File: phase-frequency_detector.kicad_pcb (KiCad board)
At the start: 2 copper layers, 160 x 100 mm, 89 parts, among them J1 REF, J2 IN, J3 Error_Out, J4 C64AC, J5 Switch, J6 Fast_Out, U1 HMC439QS16G, U2 LT3045EMSE, U3 LT3094EMSE, U4 ADA4896-2ARMZ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

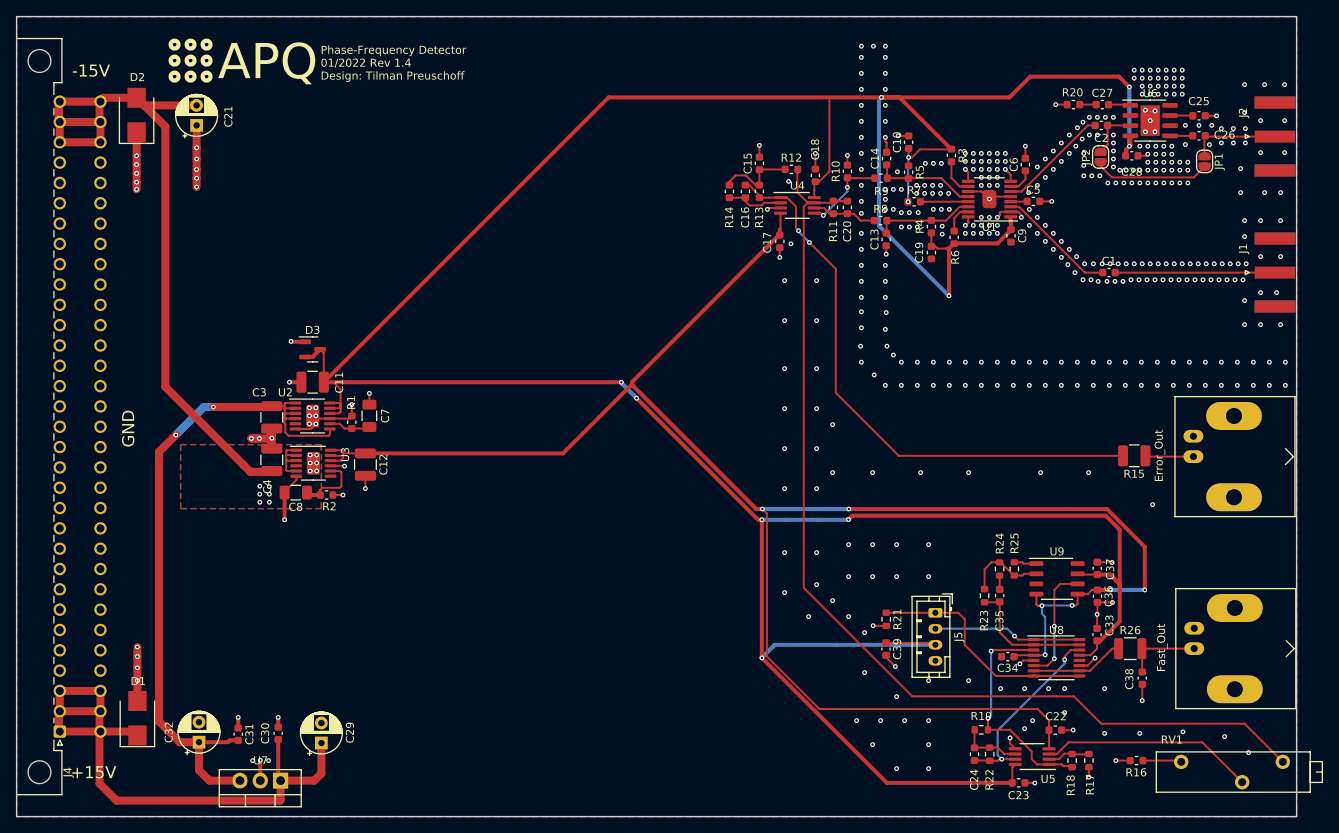
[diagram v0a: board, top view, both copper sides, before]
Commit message: Remove solder paste from DNF footprints.
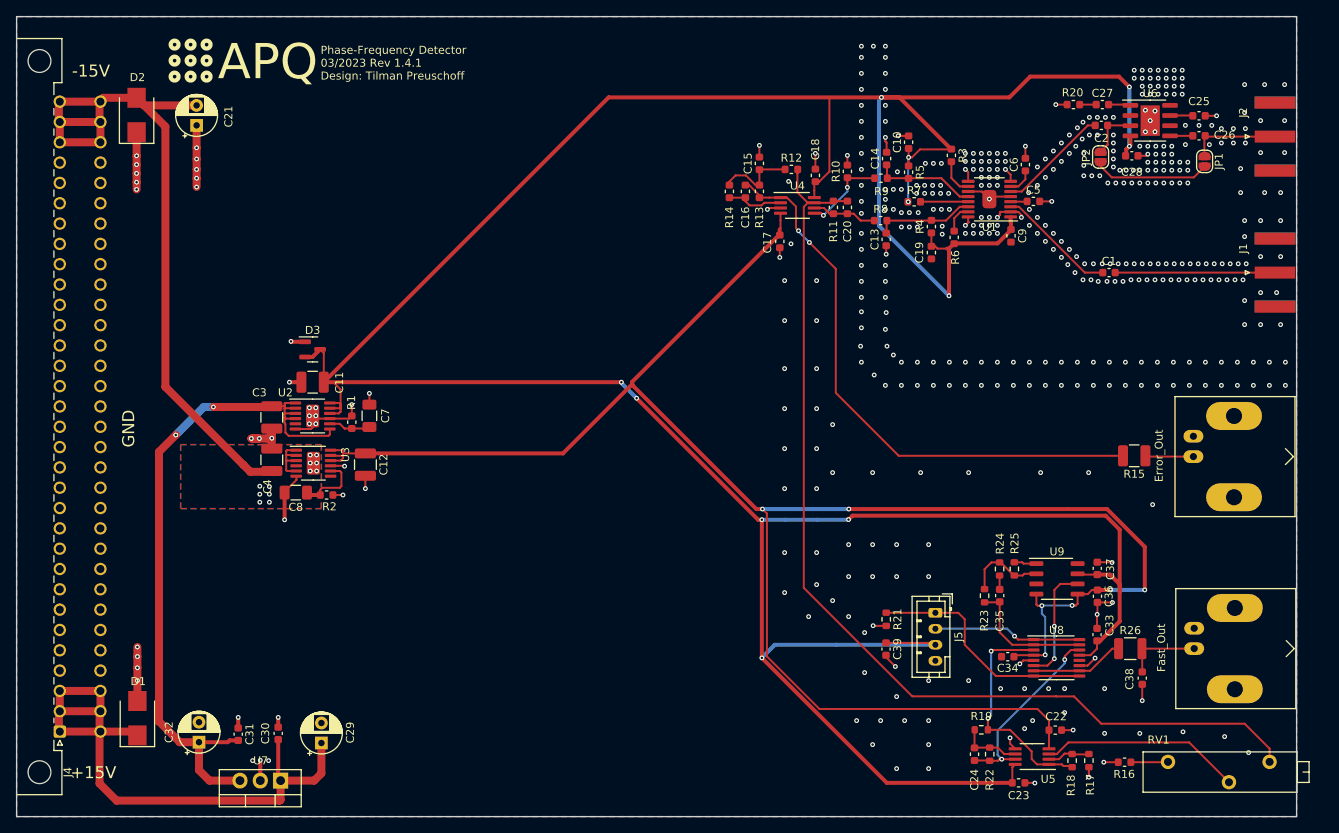
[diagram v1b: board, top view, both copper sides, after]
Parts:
- U1: footprint footprints:QSOP-16_3.9x4.9mm_P0.635mm_EP_2.3mmx1.75mm -> footprints:QSOP-16_3.9x4.9mm_P0.635mm_EP_2.3mmx1.75mm_DNF
- U6: footprint Package_SO:SOIC-8-1EP_3.9x4.9mm_P1.27mm_EP2.41x3.81mm -> footprints:SOIC-8-1EP_3.9x4.9mm_P1.27mm_EP2.41x3.81mm_DNF
- moved RV1 1.66 mm to (213.9, 143.2)
- moved R16 1.52 mm to (208.5, 143.2)
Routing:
- net Net-(RV1-Pad2): track 26.8 -> 25.2 mm
- net /Fast PD regulator/error_sig: track 127.0 -> 126.3 mm
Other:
- board text added: "Phase-Frequency Detector 03/2023 Rev 1.4.1 Design: Tilman Preuschoff"
- board text removed: "Phase-Frequency Detector 01/2022 Rev 1.4 Design: Tilman Preuschoff"

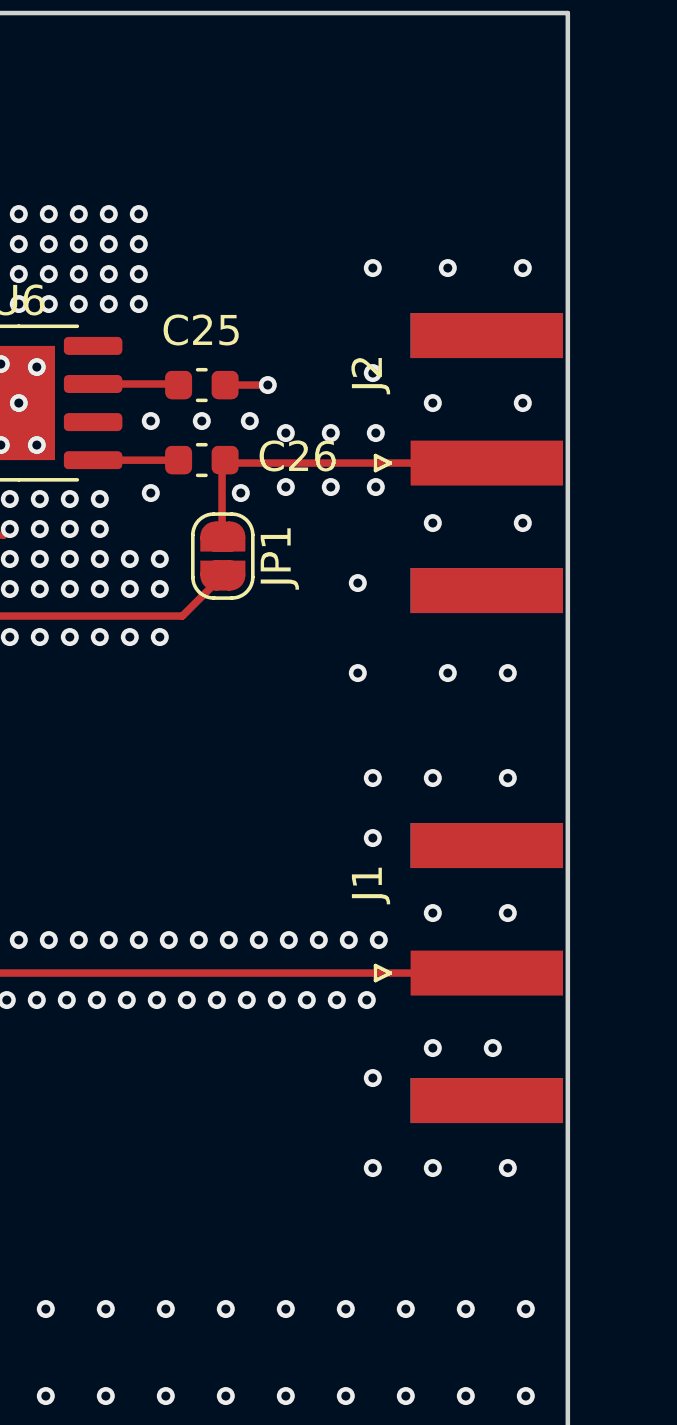
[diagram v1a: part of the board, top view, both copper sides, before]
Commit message: Add 3D models
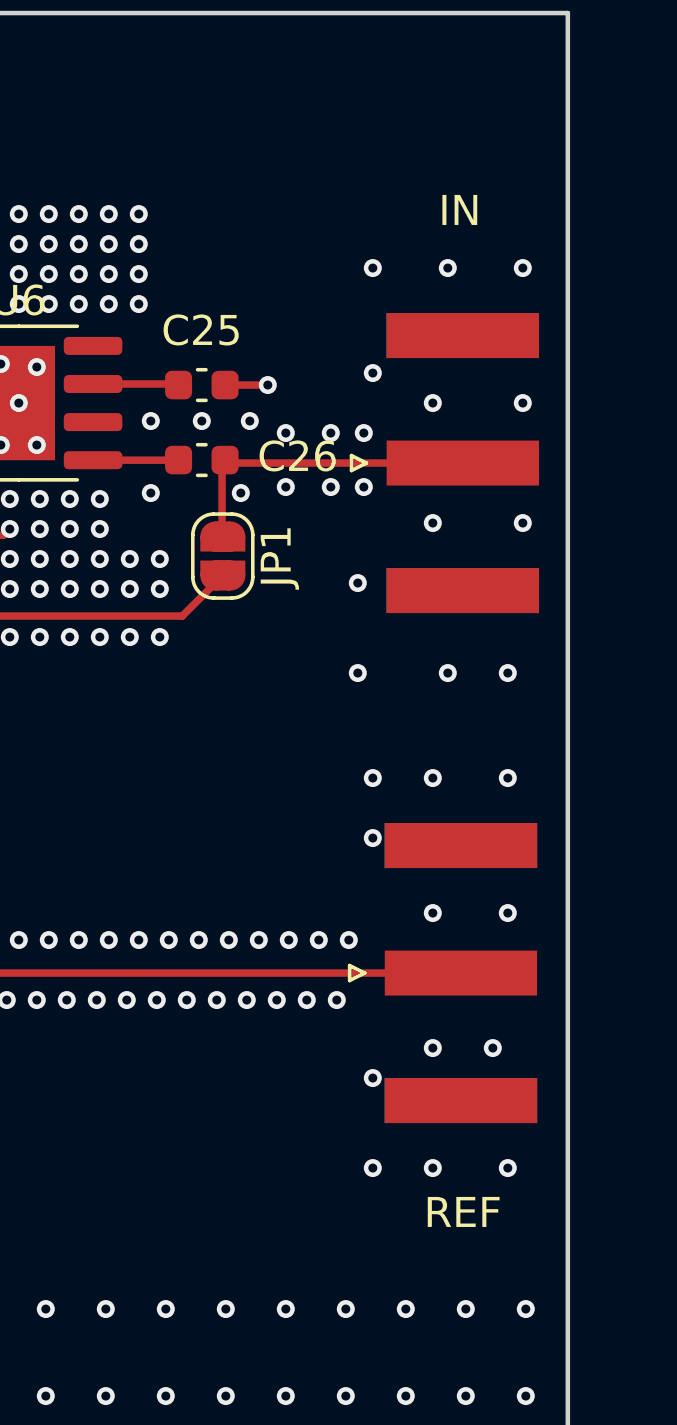
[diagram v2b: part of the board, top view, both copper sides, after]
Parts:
- moved J1 0.86 mm to (226.4, 82.0)
- moved J2 0.80 mm to (226.5, 65.0)
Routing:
- net GND: vias 469 -> 467
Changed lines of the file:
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@@
     (pad "3" thru_hole circle locked (at -12.7 0 180) (size 1.8 1.8) (drill 1) (layers *.Cu *.Mask)
       (net 32 "/Fast PD regulator/error_sig") (pinfunction "3") (pintype "passive"))
-    (model "${KISYS3DMOD}/Potentiometer_THT.3dshapes/Potentiometer_Vishay_43_Horizontal.wrl"
+    (model "${KICAD6_3DMODEL_DIR}/Potentiometer_THT.3dshapes/Potentiometer_Bourns_3005_Horizontal.step"
       (offset (xyz 0 0 0))
       (scale (xyz 1 1 1))
@@
     (pad "c32" thru_hole circle locked (at 78.74 5.08 90) (size 1.55 1.55) (drill 1) (layers *.Cu *.Mask)
       (net 20 "IN") (pinfunction "Pin_c32") (pintype "passive"))
-    (model "${KICAD6_3DMODEL_DIR}/Connector_DIN.3dshapes/DIN41612_C_2x32_Male_Horizontal_THT.wrl"
+    (model "${KIPRJMOD}/3D-models/DIN41612_C_2x32_Male_Horizontal_THT.wrl"
       (offset (xyz 0 0 0))
       (scale (xyz 1 1 1))
@@
       (rotate (xyz 0 0 0))
     )
+    (model "${KICAD6_3DMODEL_DIR}/Package_SO.3dshapes/SOIC-8-1EP_3.9x4.9mm_P1.27mm_EP2.35x2.35mm.wrl"
+      (offset (xyz 0 0 0))
+      (scale (xyz 1 1 1))
+      (rotate (xyz 0 0 0))
+    )
   )
   (footprint "Capacitor_THT:CP_Radial_D5.0mm_P2.50mm" (layer "F.Cu")
@@
     (pad "8" smd roundrect locked (at 2.575 -1.905) (size 1.75 0.6) (layers "F.Cu" "F.Paste" "F.Mask") (roundrect_rratio 0.25)
       (net 49 "unconnected-(U9-Pad8)") (pinfunction "~{SHDN}") (pintype "input+no_connect"))
-    (model "${KISYS3DMOD}/Package_SO.3dshapes/SO-8_3.9x4.9mm_P1.27mm.wrl"
+    (model "${KICAD6_3DMODEL_DIR}/Package_SO.3dshapes/SOIC-8-1EP_3.9x4.9mm_P1.27mm_EP2.35x2.35mm.wrl"
       (offset (xyz 0 0 0))
       (scale (xyz 1 1 1))
@@
   )
   (footprint "Connector_Coaxial:SMA_Amphenol_132289_EdgeMount" (layer "F.Cu")
-    (at 227.3 82)
+    (at 226.4375 82)
     (descr "http://www.amphenolrf.com/132289.html")
     (tags "SMA")
@@
     (property "Sheetname" "")
     (attr smd)
-    (fp_text reference "J1" (at -3.96 -3 90) (layer "F.SilkS")
+    (fp_text reference "J1" (at -3.96 -3 90) (layer "F.SilkS") hide
       (effects (font (size 1 1) (thickness 0.15)))
     )
-    (fp_text value "REF" (at 5 6) (layer "F.Fab")
+    (fp_text value "REF" (at 0.0625 8) (layer "F.SilkS")
       (effects (font (size 1 1) (thickness 0.15)))
     )
@@
     (pad "2" smd rect locked (at 0 -4.25 90) (size 1.5 5.08) (layers "B.Cu" "B.Paste" "B.Mask")
       (net 4 "GND") (pinfunction "Ext") (pintype "passive"))
-    (model "${KISYS3DMOD}/Connector_Coaxial.3dshapes/SMA_Amphenol_132289_EdgeMount.wrl"
-      (offset (xyz 0 0 0))
+    (model "${KIPRJMOD}/3D-models/132289.stp"
+      (offset (xyz 3.5 0 0.4))
       (scale (xyz 1 1 1))
-      (rotate (xyz 0 0 0))
+      (rotate (xyz -90 0 180))
     )
   )
   (footprint "Connector_Coaxial:SMA_Amphenol_132289_EdgeMount" (layer "F.Cu")
-    (at 227.3 65)
+    (at 226.5 65)
     (descr "http://www.amphenolrf.com/132289.html")
     (tags "SMA")
@@
     (property "Sheetname" "")
     (attr smd)
-    (fp_text reference "J2" (at -3.96 -3 90) (layer "F.SilkS")
+    (fp_text reference "J2" (at -3.96 -3 90) (layer "F.SilkS") hide
       (effects (font (size 1 1) (thickness 0.15)))
     )
-    (fp_text value "IN" (at 5 6) (layer "F.Fab")
+    (fp_text value "IN" (at -0.1 -8.4) (layer "F.SilkS")
       (effects (font (size 1 1) (thickness 0.15)))
     )
@@
     (pad "2" smd rect locked (at 0 -4.25 90) (size 1.5 5.08) (layers "B.Cu" "B.Paste" "B.Mask")
       (net 4 "GND") (pinfunction "Ext") (pintype "passive"))
-    (model "${KISYS3DMOD}/Connector_Coaxial.3dshapes/SMA_Amphenol_132289_EdgeMount.wrl"
-      (offset (xyz 0 0 0))
+    (model "${KIPRJMOD}/3D-models/132289.stp"
+      (offset (xyz 3.5 0 0.4))
       (scale (xyz 1 1 1))
-      (rotate (xyz 0 0 0))
+      (rotate (xyz -90 0 180))
     )
   )
@@
     (pad "2" thru_hole oval locked (at 5.08 -5.08 270) (size 3.5 7) (drill 2.01) (layers *.Cu *.Mask)
       (net 4 "GND") (pinfunction "Ext") (pintype "passive"))
-    (model "${KISYS3DMOD}/Connector_Coaxial.3dshapes/BNC_Amphenol_B6252HB-NPP3G-50_Horizontal.wrl"
-      (offset (xyz 0 0 0))
+    (model "${KIPRJMOD}/3D-models/CONBNC002.stp"
+      (offset (xyz 0 5 0))
       (scale (xyz 1 1 1))
-      (rotate (xyz 0 0 0))
+      (rotate (xyz -90 0 180))
     )
   )
@@
     (pad "2" thru_hole oval locked (at -2.54 0 270) (size 1.6 2.5) (drill 0.89) (layers *.Cu *.Mask)
       (net 4 "GND") (pinfunction "Ext") (pintype "passive"))
-    (model "${KISYS3DMOD}/Connector_Coaxial.3dshapes/BNC_Amphenol_B6252HB-NPP3G-50_Horizontal.wrl"
-      (offset (xyz 0 0 0))
+    (model "${KIPRJMOD}/3D-models/CONBNC002.stp"
+      (offset (xyz 0 5 0))
       (scale (xyz 1 1 1))
-      (rotate (xyz 0 0 0))
+      (rotate (xyz -90 0 180))
     )
   )
@@
   (via (at 221.3 82.9) (size 0.6) (drill 0.3) (layers "F.Cu" "B.Cu") (net 4))
   (via (at 222.3 82.9) (size 0.6) (drill 0.3) (layers "F.Cu" "B.Cu") (net 4))
-  (via (at 223.3 82.9) (size 0.6) (drill 0.3) (layers "F.Cu" "B.Cu") (net 4))
   (via (at 212.7 59.7) (size 0.6) (drill 0.3) (layers "F.Cu" "B.Cu") (net 4))
   (via (at 213.7 59.7) (size 0.6) (drill 0.3) (layers "F.Cu" "B.Cu") (net 4))
@@
   (via (at 220.6 64) (size 0.6) (drill 0.3) (layers "F.Cu" "B.Cu") (net 4))
   (via (at 222.1 64) (size 0.6) (drill 0.3) (layers "F.Cu" "B.Cu") (net 4))
-  (via (at 223.6 64) (size 0.6) (drill 0.3) (layers "F.Cu" "B.Cu") (net 4))
+  (via (at 223.2 64) (size 0.6) (drill 0.3) (layers "F.Cu" "B.Cu") (net 4))
   (via (at 219.1 66) (size 0.6) (drill 0.3) (layers "F.Cu" "B.Cu") (net 4))
   (via (at 220.6 65.8) (size 0.6) (drill 0.3) (layers "F.Cu" "B.Cu") (net 4))
   (via (at 222.1 65.8) (size 0.6) (drill 0.3) (layers "F.Cu" "B.Cu") (net 4))
-  (via (at 223.6 65.8) (size 0.6) (drill 0.3) (layers "F.Cu" "B.Cu") (net 4))
+  (via (at 223.2 65.8) (size 0.6) (drill 0.3) (layers "F.Cu" "B.Cu") (net 4))
   (via (at 199.6 66.8) (size 0.6) (drill 0.3) (layers "F.Cu" "B.Cu") (net 4))
   (via (at 104.3 90.6) (size 0.6) (drill 0.3) (layers "F.Cu" "B.Cu") (net 4))
@@
   (via (at 183 107) (size 0.6) (drill 0.3) (layers "F.Cu" "B.Cu") (net 4))
   (via (at 166 117) (size 0.6) (drill 0.3) (layers "F.Cu" "B.Cu") (net 4))
-  (via (at 223.7 80.9) (size 0.6) (drill 0.3) (layers "F.Cu" "B.Cu") (net 4))
   (via (at 178.6 53.7) (size 0.6) (drill 0.3) (layers "F.Cu" "B.Cu") (net 4))
   (via (at 206.4 70.8) (size 0.6) (drill 0.3) (layers "F.Cu" "B.Cu") (net 4))

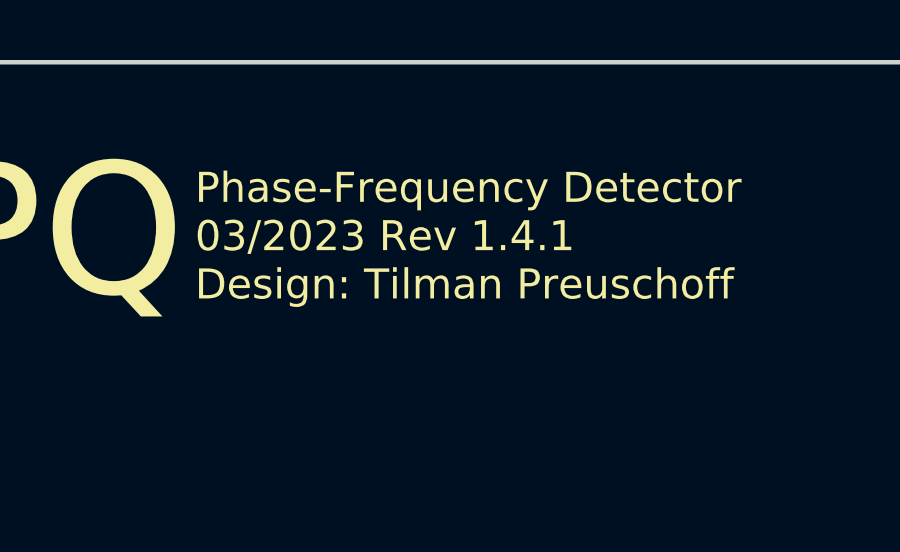
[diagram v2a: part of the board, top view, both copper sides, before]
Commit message: Add assembly instructions
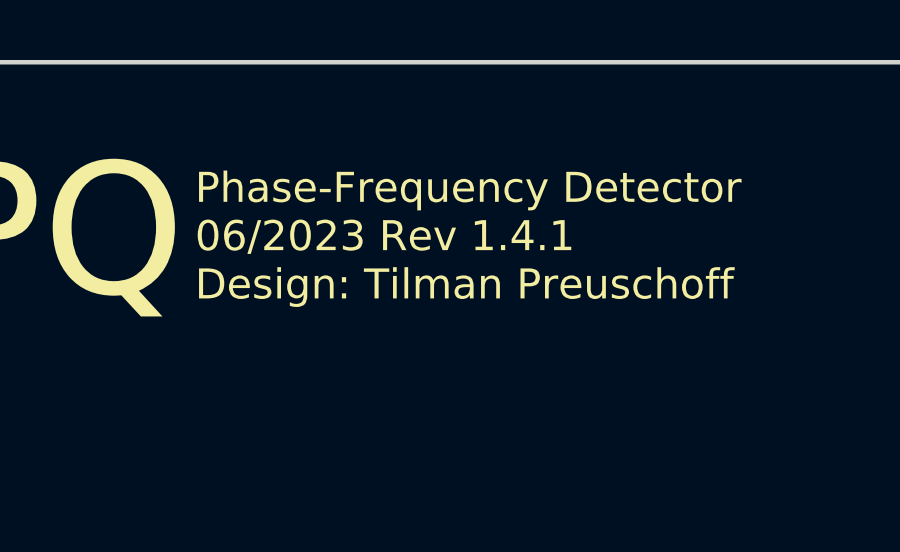
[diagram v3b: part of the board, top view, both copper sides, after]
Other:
- board text added: "Manufacturing instructions: - Material FR-4 - Finished thickness: 1.57 mm ± 0.13 mm - Surface finish: HASL lead-free - PCBs are to be RoHS compliant - Do not edit artwork, e.g. to add logos or order numbers - Clean to meet IPC J-STD-001E, Class 2 or better after assembly For assembled PCBs, use the following TARIC code for shipping: 90304000"
- board text added: "Phase-Frequency Detector 06/2023 Rev 1.4.1 Design: Tilman Preuschoff"
- board text added: "Place edge-mount SMA connectors within +/-0.3mm centred on central pad"
- board text removed: "Phase-Frequency Detector 03/2023 Rev 1.4.1 Design: Tilman Preuschoff"
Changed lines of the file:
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@@
   (title_block
     (title "Phase-Frequency Detector")
-    (date "2023-03-22")
+    (date "2023-06-16")
     (rev "1.4.1")
     (company "Atoms Photons Quanta, Institut für Angewandte Physik, TU Darmstadt")
@@
     (descr "http://www.amphenolrf.com/132289.html")
     (tags "SMA")
-    (property "MFN" "Linx Technologies ")
-    (property "PN" "CONREVSMA006.062-G ")
+    (property "MFN" "Amphenol")
+    (property "PN" "132289")
     (property "Sheetfile" "phase-frequency_detector.kicad_sch")
     (property "Sheetname" "")
@@
     (descr "http://www.amphenolrf.com/132289.html")
     (tags "SMA")
-    (property "MFN" "Linx Technologies ")
-    (property "PN" "CONREVSMA006.062-G ")
+    (property "MFN" "Amphenol")
+    (property "PN" "132289")
     (property "Sheetfile" "phase-frequency_detector.kicad_sch")
     (property "Sheetname" "")
@@
   (gr_line (start 70 150) (end 230 150) (layer "Edge.Cuts") (width 0.15))
   (gr_line (start 230 150) (end 230 50) (layer "Edge.Cuts") (width 0.15))
-  (gr_text "Phase-Frequency Detector\n03/2023 Rev 1.4.1\nDesign: Tilman Preuschoff" (at 108 55.8) (layer "F.SilkS")
+  (gr_text "Phase-Frequency Detector\n06/2023 Rev 1.4.1\nDesign: Tilman Preuschoff" (at 108 55.8) (layer "F.SilkS")
     (effects (font (size 1 1) (thickness 0.2)) (justify left))
   )
@@
     (effects (font (size 1.5 1.5) (thickness 0.3)))
   )
+  (gr_text "Place edge-mount SMA connectors \nwithin +/-0.3mm centred\non central pad" (at 242.8 63.9) (layer "F.Fab")
+    (effects (font (size 1.5 1.5) (thickness 0.3)) (justify left))
+  )
+  (gr_text "Manufacturing instructions:\n- Material FR-4\n- Finished thickness: 1.57 mm ± 0.13 mm\n- Surface finish: HASL lead-free\n- PCBs are to be RoHS compliant\n- Do not edit artwork, e.g. to add logos\n   or order numbers\n- Clean to meet IPC J-STD-001E, Class 2\n   or better after assembly\n\nFor assembled PCBs, use the \nfollowing TARIC code for shipping:\n90304000" (at 231.3 32.6) (layer "F.Fab")
+    (effects (font (size 1.5 1.5) (thickness 0.3)) (justify left))
+  )
   (segment (start 203.5343 82) (end 195.3043 73.77) (width 0.25) (layer "F.Cu") (net 1))
